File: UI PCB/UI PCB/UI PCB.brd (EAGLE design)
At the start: 67.3 x 50.5 mm, 23 parts, among them IC1 MCP23S17SP, IC2 MCP23S17SP, X1 JST-XH-02-PIN-ROUND-PAD, X2 JST-XH-02-PIN-ROUND-PAD, X3 JST-XH-02-PIN-ROUND-PAD, X4 JST-XH-02-PIN-ROUND-PAD, X5 JST-XH-05-PIN-ROUND-PAD, X6 JST-XH-05-PIN-ROUND-PAD, X7 JST-XH-05-PIN-ROUND-PAD, X8 JST-XH-05-PIN-ROUND-PAD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

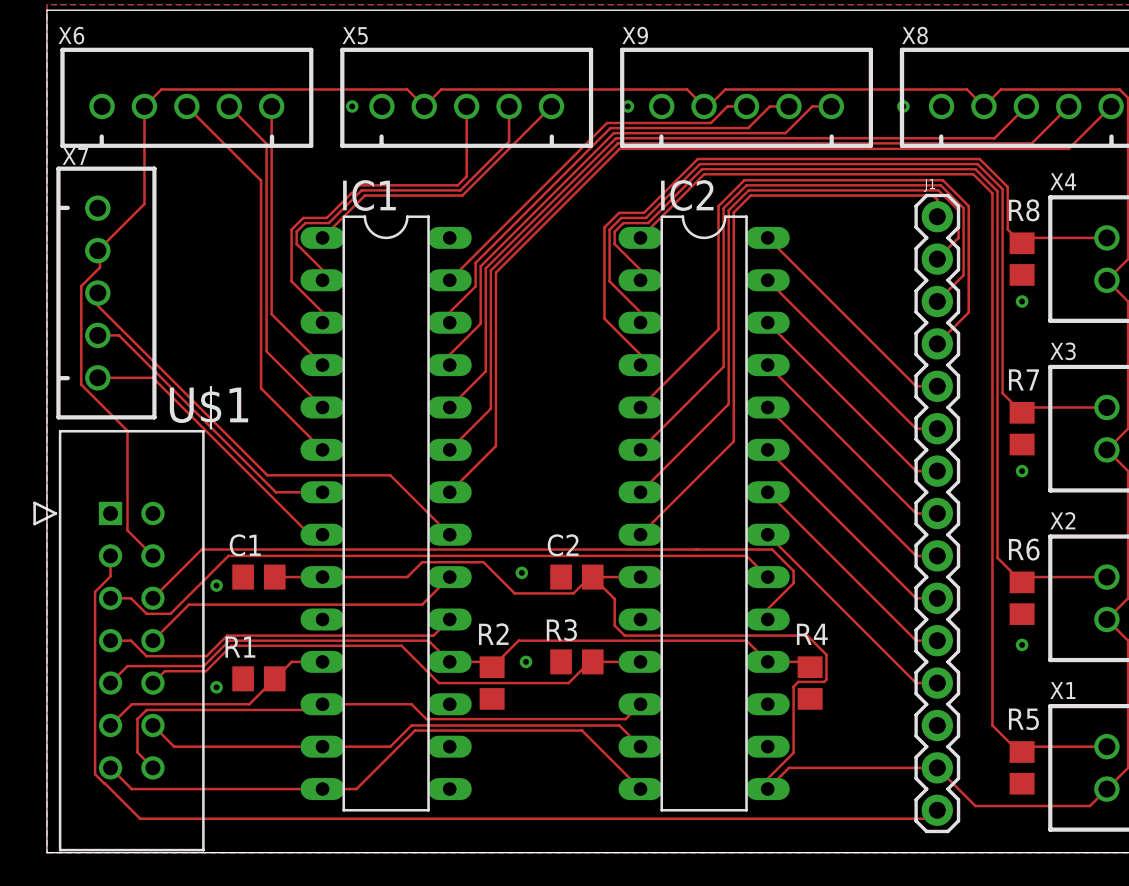
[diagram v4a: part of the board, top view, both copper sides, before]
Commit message: revieuw met ruben mondelijk gedaan, wat aangepast - nieuwe versie is dit.
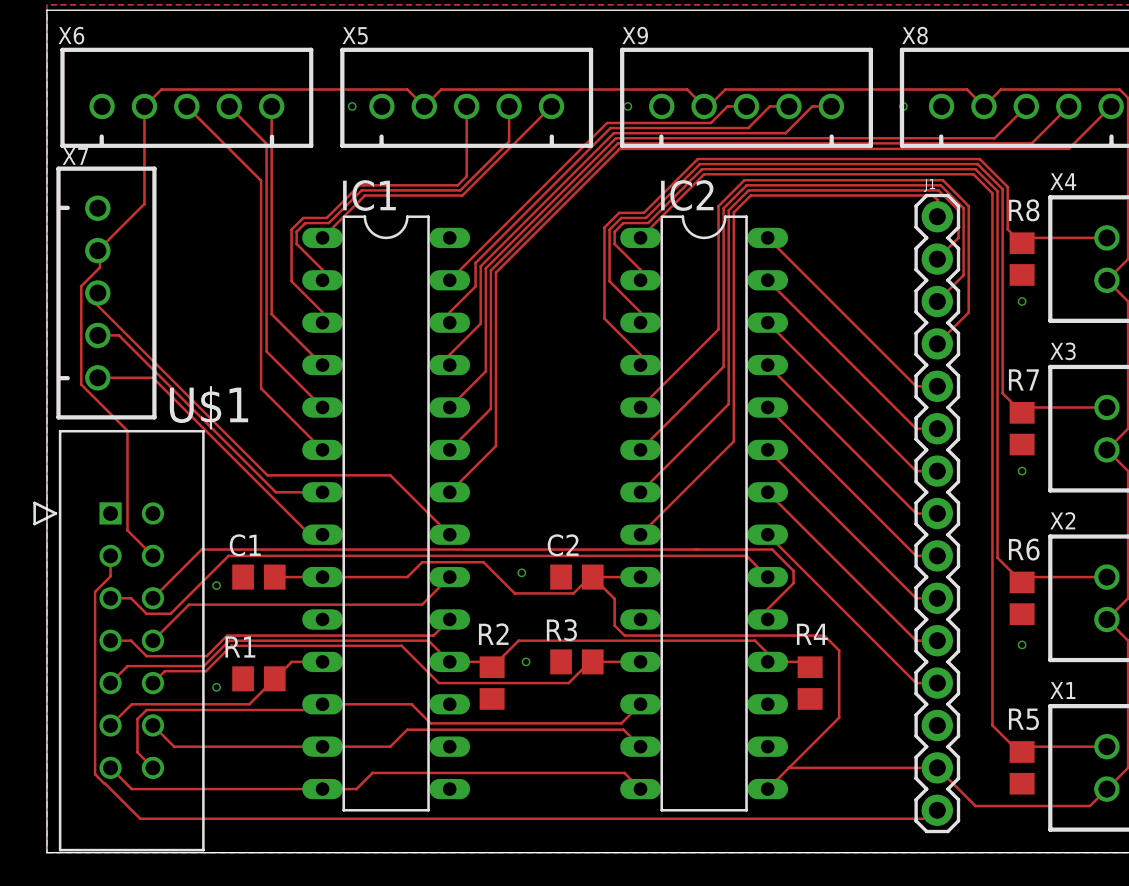
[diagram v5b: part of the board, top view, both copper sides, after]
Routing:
- net MISO: track 35.2 -> 33.1 mm
- net 3V3: track 210.6 -> 209.3 mm

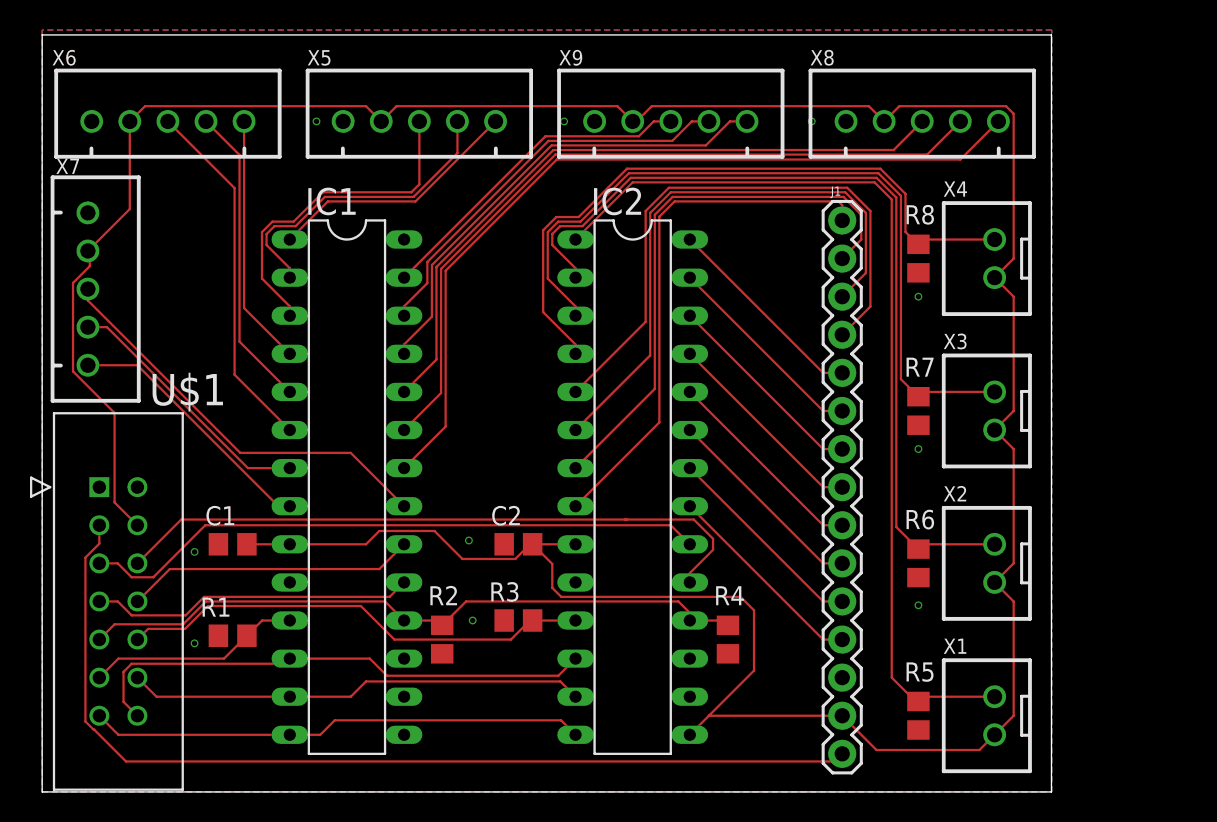
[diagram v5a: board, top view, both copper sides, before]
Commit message: some changes to PCB design, thicker power supply lines
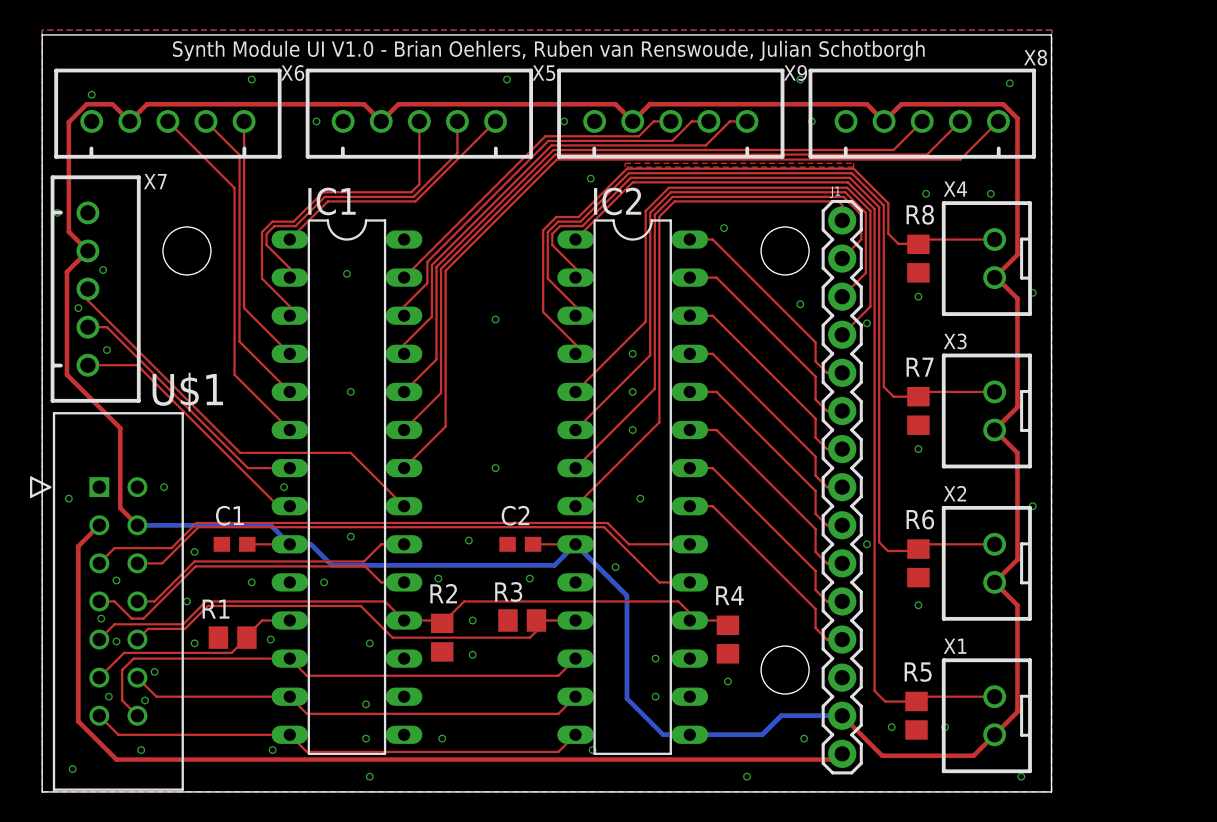
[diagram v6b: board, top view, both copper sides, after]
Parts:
- C1, C2: value (none) -> 100n; device rcl:C0805 -> rcl:C0603
- moved R3 0.25 mm to (32.0, 11.4)
- moved R5 0.13 mm to (58.3, 5.08)
- moved C1 0.13 mm to (12.8, 16.5)
- moved R2 0.13 mm to (26.7, 10.3)
- moved C2 0.13 mm to (31.9, 16.5)
- moved R1 0.13 mm to (12.7, 10.3)
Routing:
- net 3V3: track 209.3 -> 219.4 mm
- net INTB2: track 43.7 -> 39.4 mm
- net INTB1: track 21.6 -> 22.7 mm
- net GPA6: track 13.8 -> 14.7 mm
- net GPA2: track 13.8 -> 14.7 mm
- net GPA3: track 13.8 -> 14.7 mm
- net GPA7: track 13.8 -> 14.6 mm
- net GPA5: track 13.8 -> 14.6 mm
- net GPA4: track 13.8 -> 14.6 mm
- net GPA1: track 13.8 -> 14.6 mm
- net GPA0: track 13.8 -> 14.6 mm
- net INTA2: track 41.7 -> 41.1 mm
- net 5V: track 65.2 -> 65.8 mm
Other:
- board text added: "Synth Module UI V1.0 - Brian Oehlers, Ruben van Renswoude, Julian Schotborgh"
